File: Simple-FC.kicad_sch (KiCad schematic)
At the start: 0 parts

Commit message: picked imu and mcu
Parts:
- added U1: RP2350A, Package_DFN_QFN:QFN-60-1EP_7x7mm_P0.4mm_EP3.4x3.4mm, symbol MCU_RaspberryPi:RP2350A
- added U3: LSM6DSM, Package_LGA:LGA-14_3x2.5mm_P0.5mm_LayoutBorder3x4y, symbol Sensor_Motion:LSM6DSM
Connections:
- new net: U1.1 (IOVDD), U1.11 (IOVDD), U1.20 (IOVDD), U1.30 (IOVDD), U1.38 (IOVDD), U1.45 (IOVDD)
- new net: U1.23 (DVDD), U1.39 (DVDD), U1.6 (DVDD)
- new net: U3.6 (GND), U3.7 (GND)

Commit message: selected parts
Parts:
- added C1, C2: 33pF, Capacitor_SMD:C_0402_1005Metric, symbol Device:C
- added C1, C3: 10uF, Capacitor_SMD:C_0603_1608Metric, symbol Device:C
- added C5: 0.1uF, Capacitor_SMD:C_0402_1005Metric, symbol Device:C
- added D1: D_Schottky, Diode_SMD:D_0402_1005Metric, symbol Device:D_Schottky
- added J1: USB_C_Receptacle_USB2.0_14P, Connector_USB:USB_C_Receptacle_HRO_TYPE-C-31-M-12, symbol Connector:USB_C_Receptacle_USB2.0_14P
- added J2: Micro_SD_Card, Connector_Card:microSD_HC_Molex_47219-2001, symbol Connector:Micro_SD_Card
- added R1, R2: 5.1K, Resistor_SMD:R_0402_1005Metric, symbol Device:R
- added R3, R5: 1K, Resistor_SMD:R_0402_1005Metric, symbol Device:R
- added R4: 10K, Resistor_SMD:R_0402_1005Metric, symbol Device:R
- added SW1: SW_Push, Button_Switch_SMD:SW_Push_SPST_NO_Alps_SKRK, symbol Switch:SW_Push
- added U2: MMC5983MA, Package_LGA:LGA-16_3x3mm_P0.5mm, symbol Simple-FC:MMC5983MA
- added U4: BMP384, Package_LGA:ST_HLGA-10_2x2mm_P0.5mm_LayoutBorder3x2y, symbol Simple-FC:BMP384
- added U5: MCP1700x-330xxTT, Package_TO_SOT_SMD:SOT-23, symbol Regulator_Linear:MCP1700x-330xxTT
- added U6: W25Q128JVS, Package_SON:Winbond_USON-8-1EP_3x2mm_P0.5mm_EP0.2x1.6mm, symbol Memory_Flash:W25Q128JVS
- added Y1: ABM8-272-T3, Crystal:Crystal_SMD_3225-4Pin_3.2x2.5mm, symbol Device:Crystal_GND24
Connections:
- new net: C2.1, R5.1, Y1.1
- new net: J1.A5 (CC1), R1.1
- new net: D1.2 (A), J1.A4 (VBUS), J1.A9 (VBUS), J1.B4 (VBUS), J1.B9 (VBUS)
- new net: J1.B5 (CC2), R2.1
- new net: C3.1, D1.1 (K), U5.3 (VI)
- new net: R3.1, SW1.2
- new net +3V3: C1.1, C5.1, R4.1, U5.2 (VO), U6.8 (VCC)
- new net GND: C1.1, C1.2, C2.2, C3.2, C5.2, J1.A1 (GND), J1.A12 (GND), J1.B1 (GND), J1.B12 (GND), J1.S1 (SHIELD), R1.2, R2.2, SW1.1, U5.1 (GND), U6.4 (GND), Y1.2, Y1.4
- new net QSPI_SCLK: U6.6 (CLK)
- new net QSPI_SD0: U6.5 (DI/IO_{0})
- new net QSPI_SD1: U6.2 (DO/IO_{1})
- new net QSPI_SD2: U6.3 (~{WP}/IO_{2})
- new net QSPI_SD3: U6.7 (~{HOLD}/~{RESET}/IO_{3})
- new net QSPI_SS: R3.2, R4.2, U6.1 (~{CS})
- new net USB_D+: J1.A6 (D+), J1.B6 (D+)
- new net USB_D-: J1.A7 (D-), J1.B7 (D-)
- new net XIN: C1.2, Y1.3
- new net XOUT: R5.2
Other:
- moved on the sheet: U1, U3

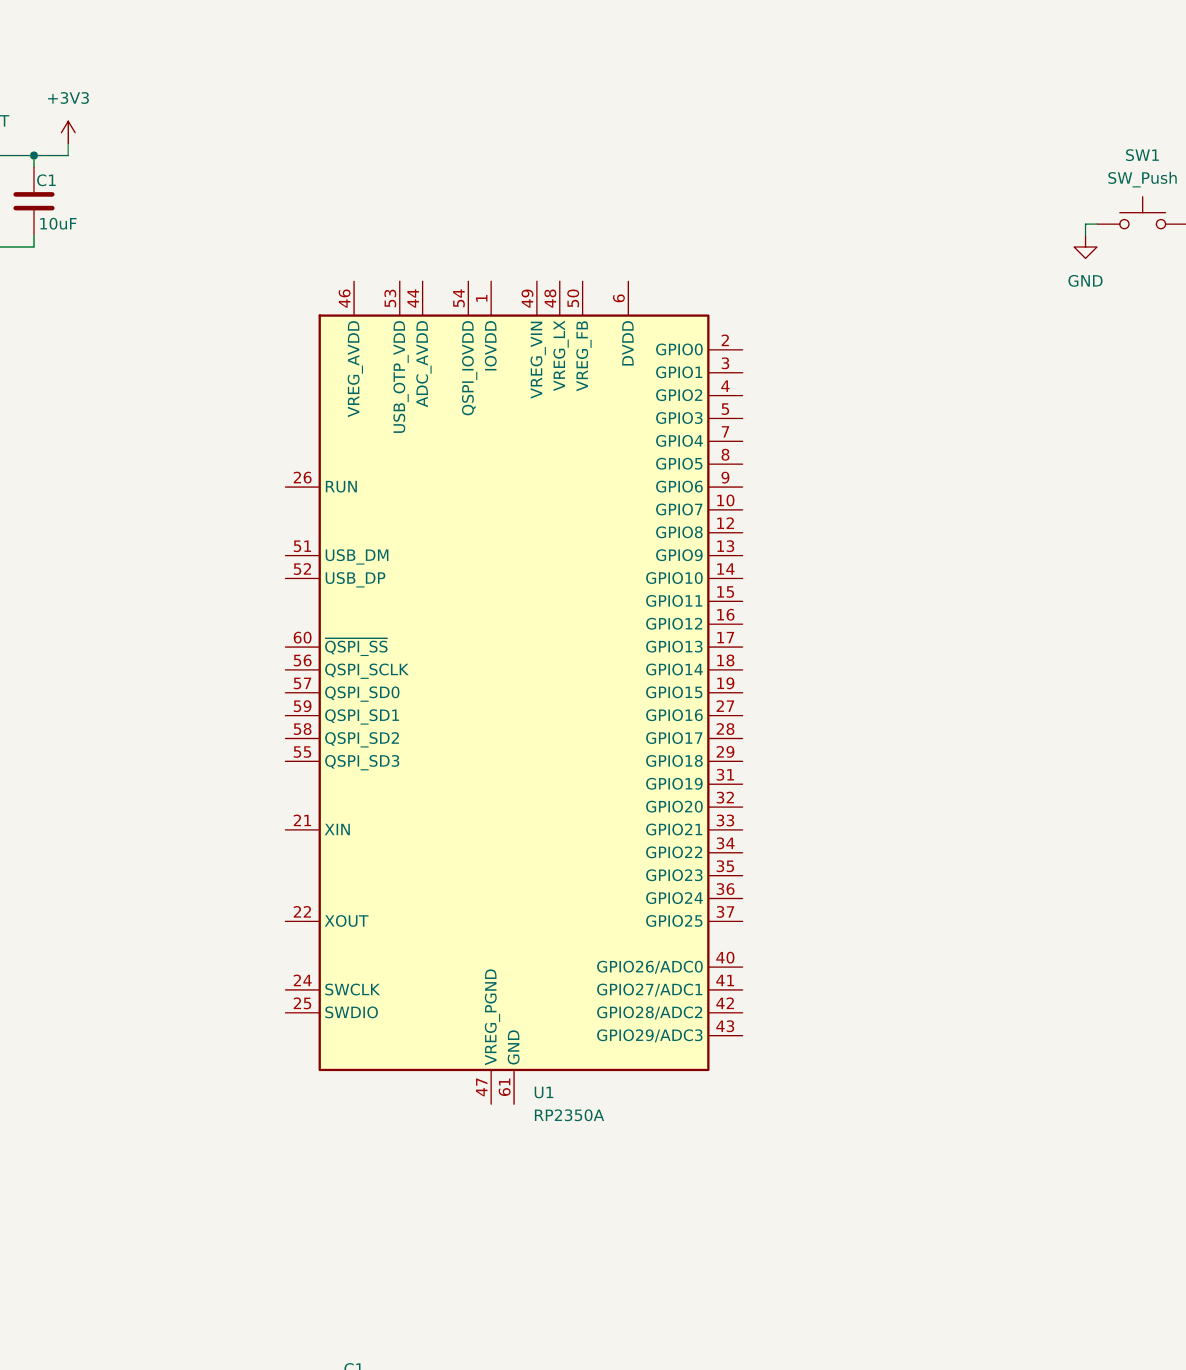
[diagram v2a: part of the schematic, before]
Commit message: added decoupling caps
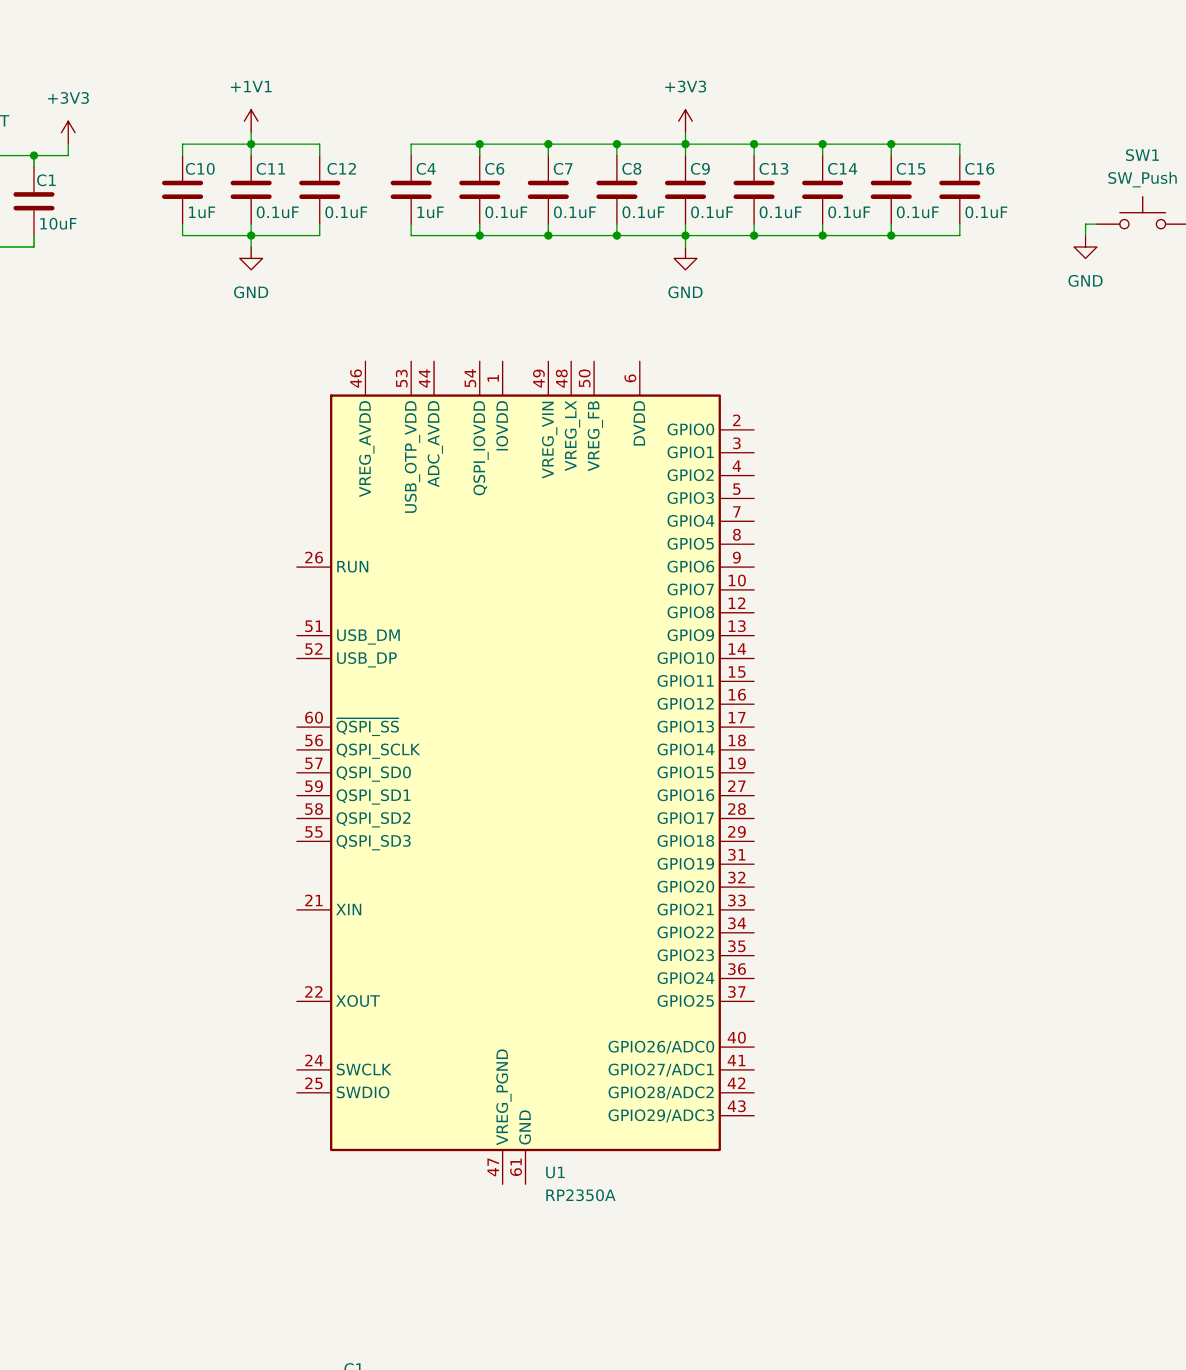
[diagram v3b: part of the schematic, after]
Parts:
- added C10, C4: 1uF, Capacitor_SMD:C_0402_1005Metric, symbol Device:C
- added C11, C12, C13, C14, C15, C16, C6, C7, C8, C9: 0.1uF, Capacitor_SMD:C_0402_1005Metric, symbol Device:C
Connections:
- net +3V3: now also C13.1, C14.1, C15.1, C16.1, C4.1, C6.1, C7.1, C8.1, C9.1
- net GND: now also C10.2, C11.2, C12.2, C13.2, C14.2, C15.2, C16.2, C4.2, C6.2, C7.2, C8.2, C9.2
- new net +1V1: C10.1, C11.1, C12.1
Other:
- moved on the sheet: U1

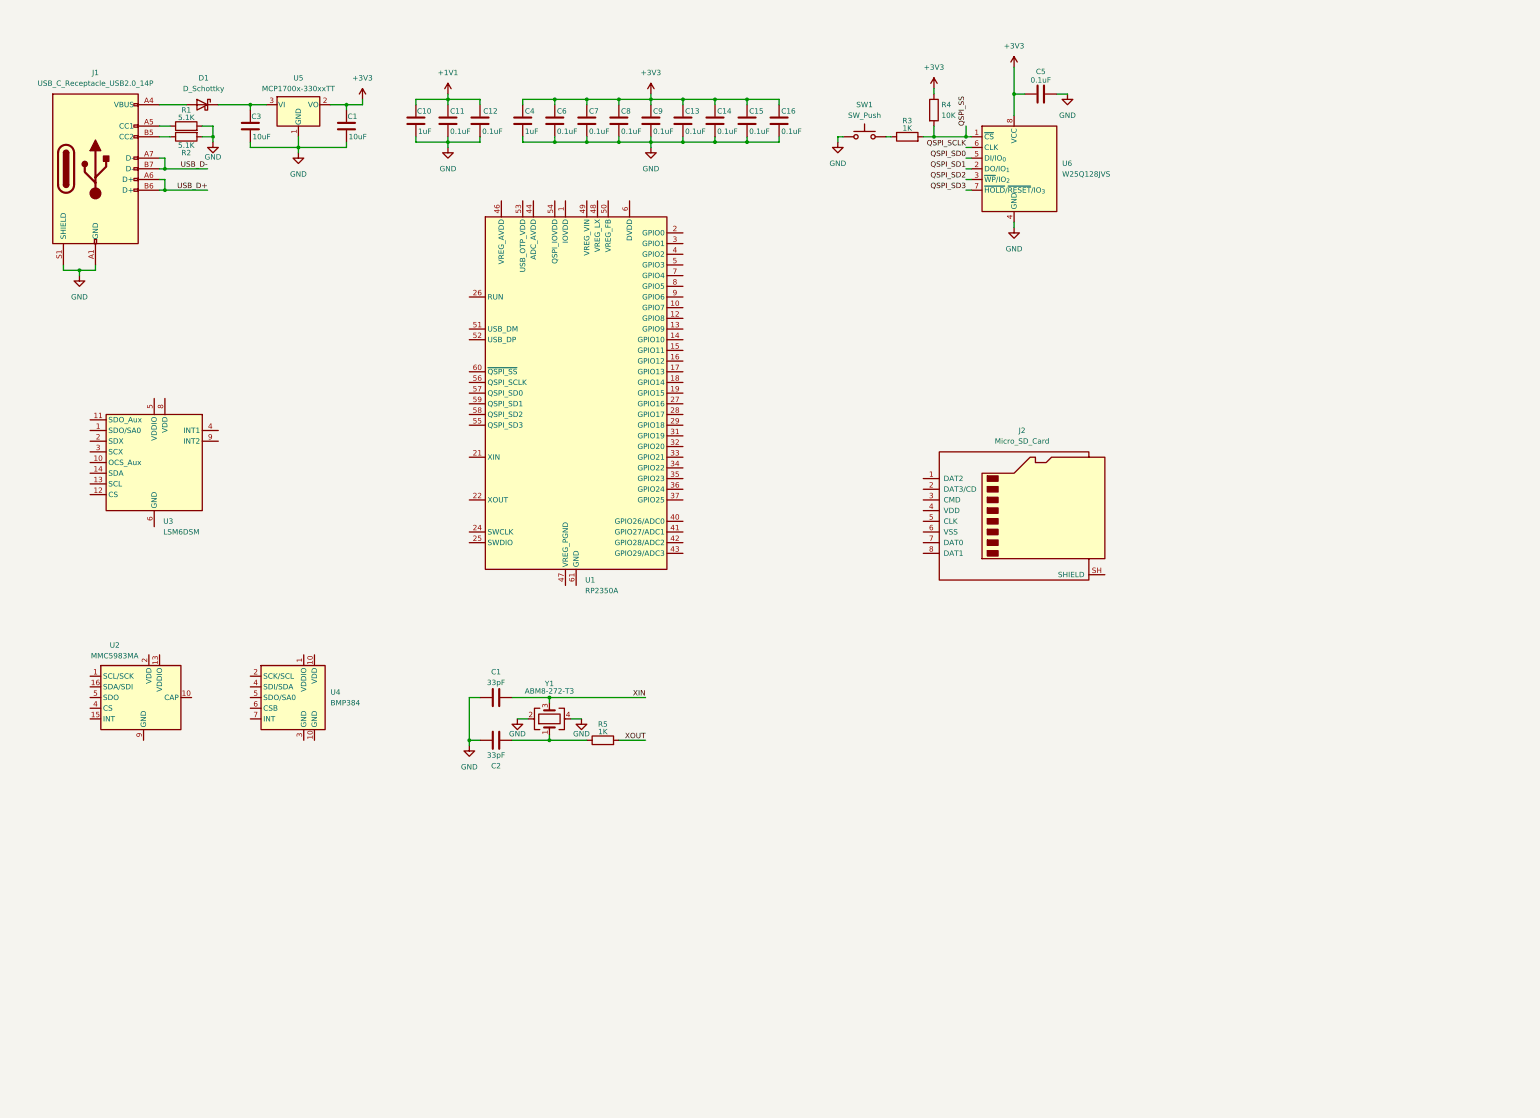
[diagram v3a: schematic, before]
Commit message: routed sensors and micro sd
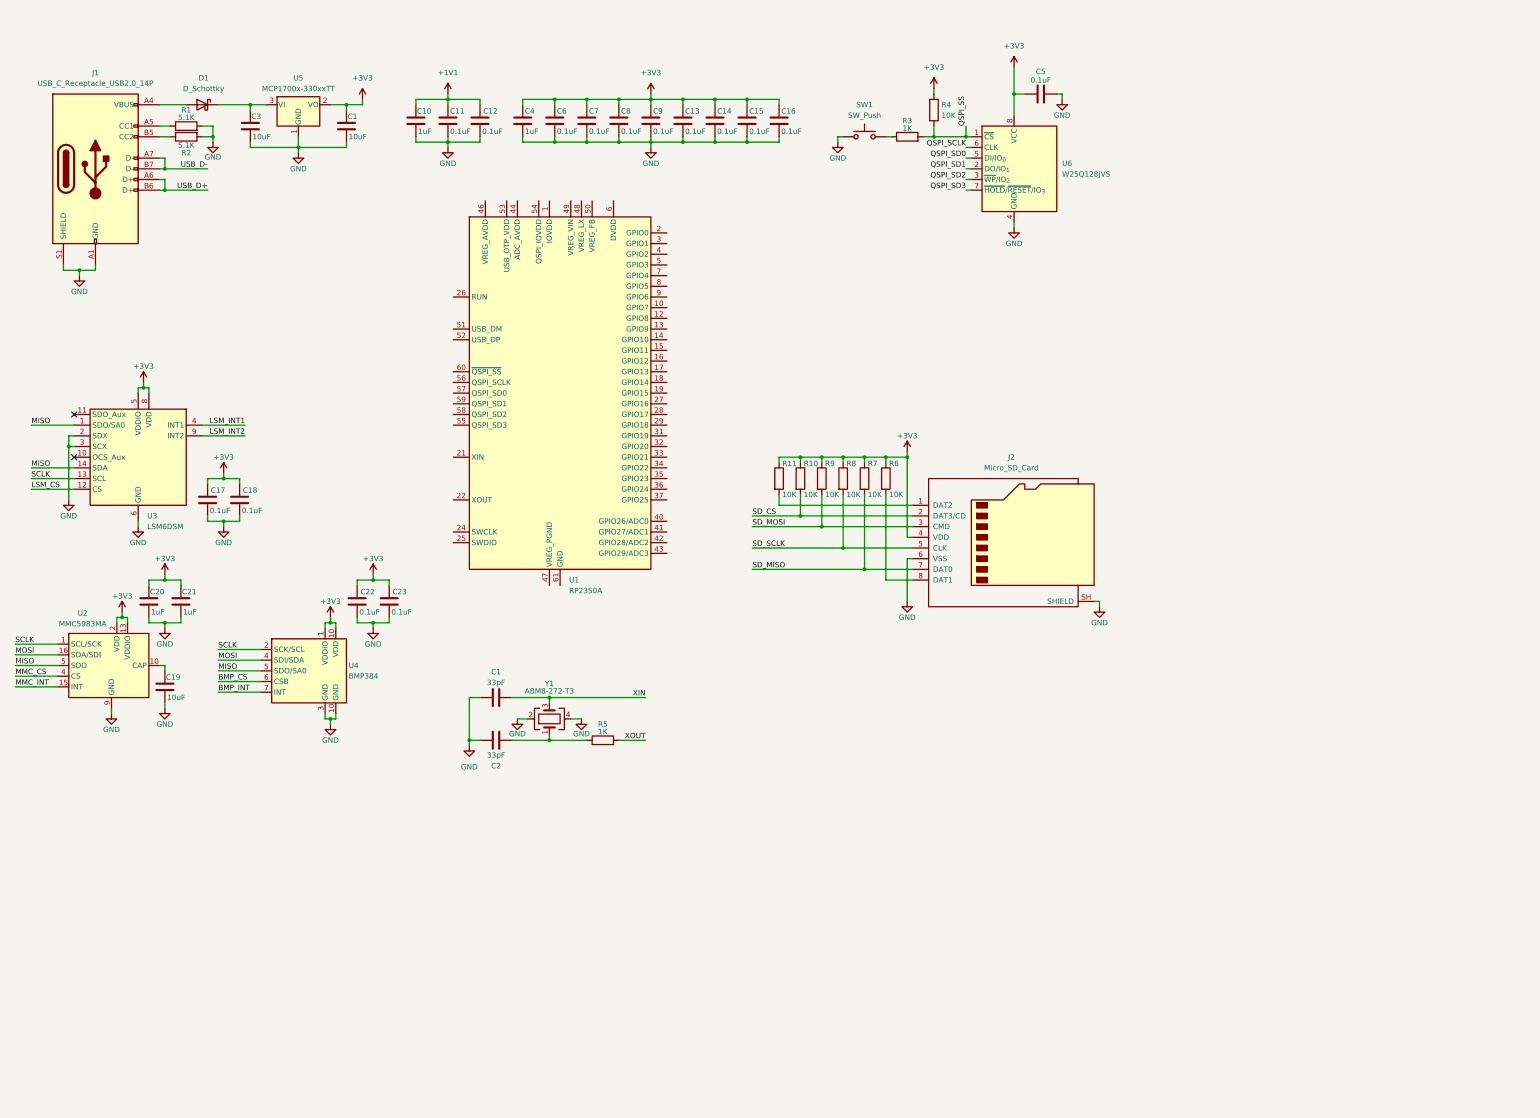
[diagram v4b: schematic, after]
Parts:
- added C17, C18, C22, C23: 0.1uF, Capacitor_SMD:C_0402_1005Metric, symbol Device:C
- added C19: 10uF, Capacitor_SMD:C_0603_1608Metric, symbol Device:C
- added C20, C21: 1uF, Capacitor_SMD:C_0402_1005Metric, symbol Device:C
- added R10, R11, R6, R7, R8, R9: 10K, Resistor_SMD:R_0402_1005Metric, symbol Device:R
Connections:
- net +3V3: now also J2.4 (VDD), U2.13 (VDDIO), U2.2 (VDD), U3.5 (VDDIO), U3.8 (VDD), U4.1 (VDDIO), U4.10 (GND), C17.1, C18.1, C20.1, C21.1, C22.1, C23.1, R10.1, R11.1, R6.1, R7.1, R8.1, R9.1
- net GND: now also J2.6 (VSS), J2.SH (SHIELD), U2.9 (GND), U3.2 (SDX), U3.3 (SCX), U3.6 (GND), U3.7 (GND), U4.10 (GND), U4.3 (GND), C17.2, C18.2, C19.2, C20.2, C21.2, C22.2, C23.2
- net SCLK: now reaches U4.2 (SCK/SCL)
- net SCLK: now also U2.1 (SCL/SCK), U3.13 (SCL)
- net MOSI: now reaches U4.4 (SDI/SDA)
- net MOSI: now also U2.16 (SDA/SDI)
- net MISO: now reaches U4.5 (SDO/SA0)
- net MISO: now also U2.5 (NC), U3.1 (SDO/SA0), U3.14 (SDA)
- net BMP_CS: now reaches U4.6 (CSB)
- net BMP_INT: now reaches U4.7 (INT)
- net at J2.1 (DAT2): now also R11.2
- net SD_CS: now reaches J2.2 (DAT3/CD)
- net SD_CS: now also R10.2
- net SD_MOSI: now reaches J2.3 (CMD)
- net SD_MOSI: now also R9.2
- net SD_SCLK: now reaches J2.5 (CLK)
- net SD_SCLK: now also R8.2
- net SD_MISO: now reaches J2.7 (DAT0)
- net SD_MISO: now also R7.2
- net at J2.8 (DAT1): now also R6.2
- net LSM_CS: now reaches U3.12 (CS)
- net LSM_INT1: now reaches U3.4 (INT1)
- net LSM_INT2: now reaches U3.9 (INT2)
- net at U2.10 (CAP): now also C19.1
- net MMC_INT: now reaches U2.15 (INT)
- net MMC_CS: now reaches U2.4 (NC)
- no-connect marks 0 -> 2
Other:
- moved on the sheet: J2, U1, U2, U3, U4

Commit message: switched to buck-boost reg
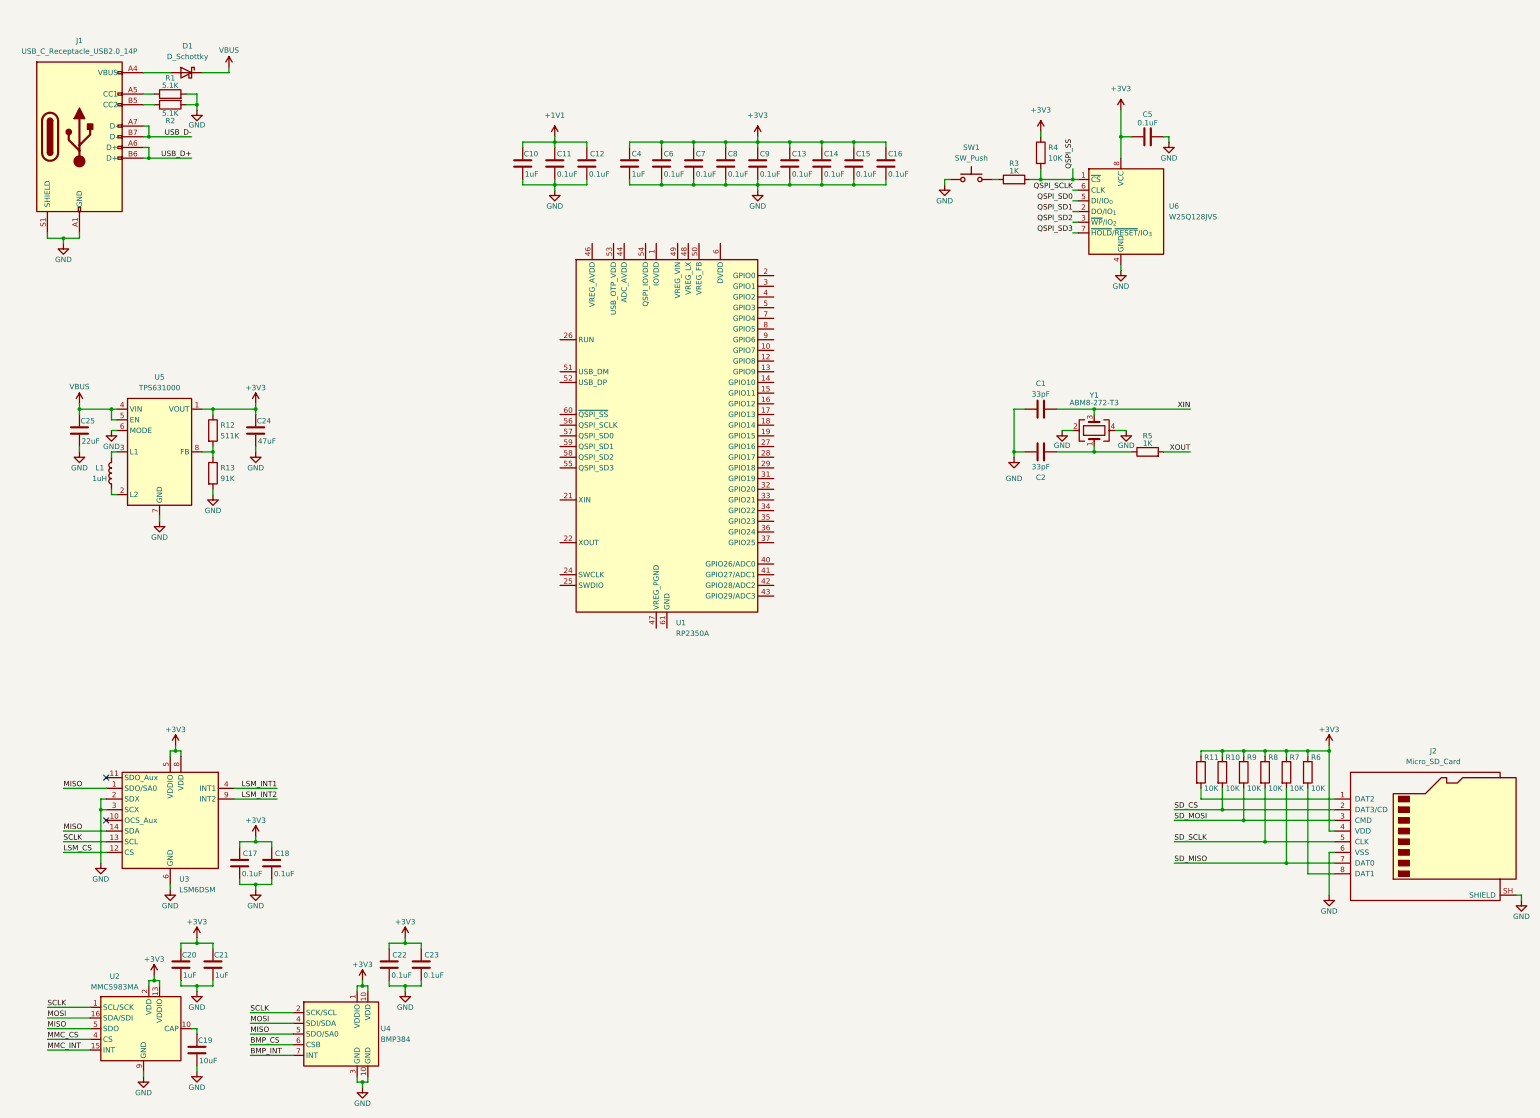
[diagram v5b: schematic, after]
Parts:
- removed C1, C3: 10uF, Capacitor_SMD:C_0603_1608Metric, symbol Device:C
- removed U5: MCP1700x-330xxTT, Package_TO_SOT_SMD:SOT-23, symbol Regulator_Linear:MCP1700x-330xxTT
- added C24: 47uF, Capacitor_SMD:C_0402_1005Metric, symbol Device:C
- added C25: 22uF, Capacitor_SMD:C_0402_1005Metric, symbol Device:C
- added L1: 1uH, Package_TO_SOT_SMD:SOT-583-8, symbol Device:L
- added R12: 511K, Resistor_SMD:R_0402_1005Metric, symbol Device:R
- added R13: 91K, Resistor_SMD:R_0402_1005Metric, symbol Device:R
- added U5: TPS631000, Package_TO_SOT_SMD:SOT-583-8, symbol Simple-FC:TPS631000
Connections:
- net +3V3: now also C24.1, R12.1, U5.1 (VOUT)
- net GND: now also C24.2, C25.2, R13.2, U5.11 (PGND), U5.6 (MODE), U5.7 (GND)
- net VBUS: now reaches D1.1 (K)
- net VBUS: now also C25.1, U5.4 (VIN), U5.5 (EN)
- new net: L1.1, U5.3 (L1)
- new net: L1.2, U5.2 (L2)
- new net: R12.2, R13.1, U5.8 (FB)
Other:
- moved on the sheet: C1, C10, C11, C12, C13, C14, C15, C16, C17, C18, C19, C2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
